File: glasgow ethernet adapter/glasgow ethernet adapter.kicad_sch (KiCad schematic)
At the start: 59 parts, among them J1 Glasgow Port, J2 RJ45_Amphenol_RJMG201K21120FR, U1 MxL86110, Y1 25 MHz

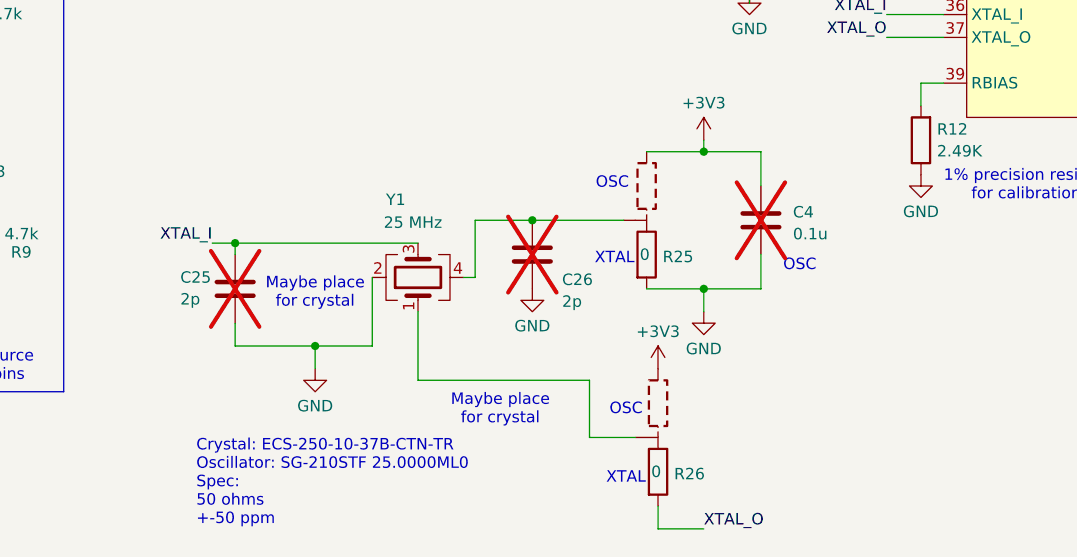
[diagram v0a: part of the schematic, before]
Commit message: export fab outputs, add note on parts sourcing
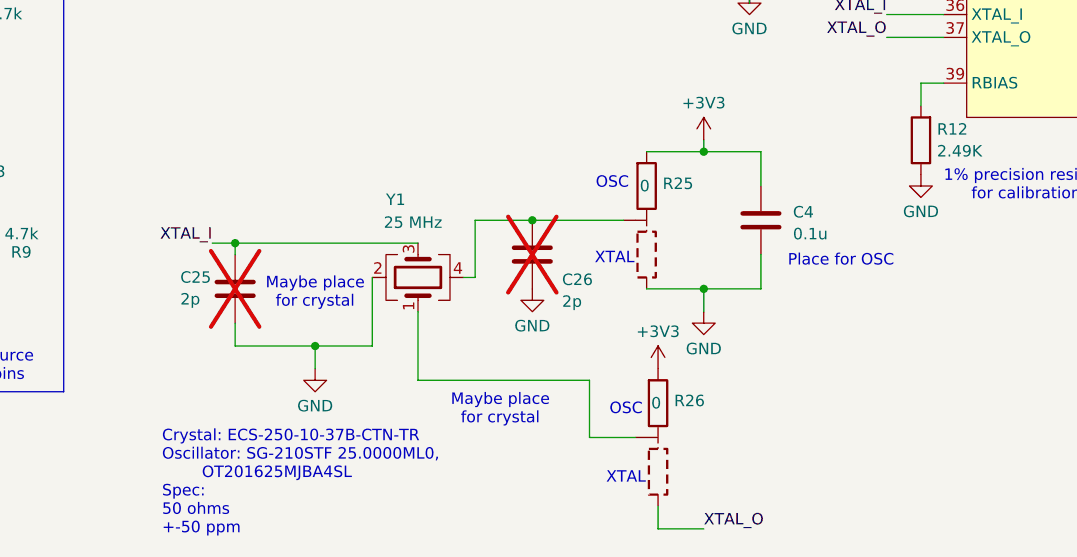
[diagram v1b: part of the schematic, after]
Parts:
- C4: now fitted
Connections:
- net +3V3: now also R25.1, R26.1; no longer R25.3, R26.3
- net GND: now also R25.3; no longer R25.1
- net XTAL_O: now also R26.3; no longer R26.1
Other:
- note added: "Crystal: ECS-250-10-37B-CTN-TR Oscillator: SG-210STF 25.0000ML0, OT201625MJBA4SL Spec: 50 ohms +-50 ppm"
- note added: "Place for OSC"
- note removed: "Crystal: ECS-250-10-37B-CTN-TR Oscillator: SG-210STF 25.0000ML0 Spec: 50 ohms +-50 ppm"
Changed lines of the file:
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@@
 	(text "OSC"
 		(exclude_from_sim no)
-		(at 160.528 166.37 0)
+		(at 139.7 157.226 0)
 		(effects
 			(font
@@
 		)
 	)
-	(text "OSC"
+	(text "Maybe place\nfor crystal\n"
 		(exclude_from_sim no)
-		(at 139.7 157.226 0)
+		(at 127.254 182.372 0)
 		(effects
 			(font
@@
 		)
 	)
-	(text "Maybe place\nfor crystal\n"
+	(text "Place for OSC"
 		(exclude_from_sim no)
-		(at 127.254 182.372 0)
+		(at 165.1 165.862 0)
 		(effects
 			(font
@@
 		)
 	)
-	(text "Crystal: ECS-250-10-37B-CTN-TR\nOscillator: SG-210STF 25.0000ML0\nSpec:\n50 ohms\n+-50 ppm"
+	(text "Crystal: ECS-250-10-37B-CTN-TR\nOscillator: SG-210STF 25.0000ML0, \n		OT201625MJBA4SL\nSpec:\n50 ohms\n+-50 ppm"
 		(exclude_from_sim no)
-		(at 93.472 190.5 0)
+		(at 89.662 190.5 0)
 		(effects
 			(font
@@
 		(in_bom yes)
 		(on_board yes)
-		(dnp yes)
+		(dnp no)
 		(property "Reference" "C4"
 			(at 159.766 160.3897 0)
@@
 	(symbol
 		(lib_id "glasgow:R-3-way")
-		(at 143.51 165.1 0)
-		(mirror x)
+		(at 143.51 157.48 0)
 		(unit 1)
 		(exclude_from_sim no)
@@
 		(dnp no)
 		(property "Reference" "R25"
-			(at 145.288 165.354 0)
+			(at 145.288 157.226 0)
 			(effects
 				(font
@@
 		)
 		(property "Value" "0"
-			(at 142.748 165.1 0)
+			(at 142.748 157.48 0)
 			(effects
 				(font
@@
 		)
 		(property "Footprint" "glasgow:R-3-Way_0402_1005Metric"
-			(at 141.732 165.1 90)
+			(at 141.732 157.48 90)
 			(effects
 				(font
@@
 		)
 		(property "Datasheet" "~"
-			(at 143.51 165.1 0)
+			(at 143.51 157.48 0)
 			(effects
 				(font
@@
 		)
 		(property "Description" "Resistor"
-			(at 143.51 165.1 0)
+			(at 143.51 157.48 0)
 			(effects
 				(font
@@
 	(symbol
 		(lib_id "glasgow:R-3-way")
-		(at 144.78 189.23 0)
-		(mirror x)
+		(at 144.78 181.61 0)
 		(unit 1)
 		(exclude_from_sim no)
@@
 		(dnp no)
 		(property "Reference" "R26"
-			(at 146.558 189.484 0)
+			(at 146.558 181.356 0)
 			(effects
 				(font
@@
 		)
 		(property "Value" "0"
-			(at 144.018 189.23 0)
+			(at 144.018 181.61 0)
 			(effects
 				(font
@@
 		)
 		(property "Footprint" "glasgow:R-3-Way_0402_1005Metric"
-			(at 143.002 189.23 90)
+			(at 143.002 181.61 90)
 			(effects
 				(font
@@
 		)
 		(property "Datasheet" "~"
-			(at 144.78 189.23 0)
+			(at 144.78 181.61 0)
 			(effects
 				(font
@@
 		)
 		(property "Description" "Resistor"
-			(at 144.78 189.23 0)
+			(at 144.78 181.61 0)
 			(effects
 				(font

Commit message: un-swap pins
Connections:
- net TRX1+: now also J2.2 (TD1+); no longer J2.10 (TD4-)
- net TRX1-: now also J2.3 (TD1-); no longer J2.9 (TD4+)
- net TRX2+: now also J2.4 (TD2+); no longer J2.8 (TD3-)
- net TRX2-: now also J2.5 (TD2-); no longer J2.7 (TD3+)
- net TRX3+: now also J2.7 (TD3+); no longer J2.5 (TD2-)
- net TRX3-: now also J2.8 (TD3-); no longer J2.4 (TD2+)
- net TRX4+: now also J2.9 (TD4+); no longer J2.3 (TD1-)
- net TRX4-: now also J2.10 (TD4-); no longer J2.2 (TD1+)
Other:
- note removed: "Pairs intentionally swapped for better routing"
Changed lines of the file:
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@@
-		)
-	)
-	(text "Pairs intentionally swapped \nfor better routing"
-		(exclude_from_sim no)
-		(at 267.208 59.69 0)
-		(effects
-			(font
-				(size 1.27 1.27)
-			)
 		)
 	)
@@
 	)
 	(label "TRX3+"
-		(at 259.08 88.9 180)
+		(at 259.08 91.44 180)
 		(fields_autoplaced yes)
 		(effects
@@
 	)
 	(label "TRX3-"
-		(at 259.08 83.82 180)
+		(at 259.08 96.52 180)
 		(fields_autoplaced yes)
 		(effects
@@
 	)
 	(label "TRX1+"
-		(at 259.08 104.14 180)
+		(at 259.08 76.2 180)
 		(fields_autoplaced yes)
 		(effects
@@
 	)
 	(label "TRX4-"
-		(at 259.08 76.2 180)
+		(at 259.08 104.14 180)
 		(fields_autoplaced yes)
 		(effects
@@
 	)
 	(label "TRX2+"
-		(at 259.08 96.52 180)
+		(at 259.08 83.82 180)
 		(fields_autoplaced yes)
 		(effects
@@
 	)
 	(label "TRX2-"
-		(at 259.08 91.44 180)
+		(at 259.08 88.9 180)
 		(fields_autoplaced yes)
 		(effects
@@
 	)
 	(label "TRX1-"
+		(at 259.08 81.28 180)
+		(fields_autoplaced yes)
+		(effects
+			(font
+				(size 1.27 1.27)
+			)
+			(justify right bottom)
+		)
+	)
+	(label "TRX4+"
 		(at 259.08 99.06 180)
 		(fields_autoplaced yes)
 		(effects
-			(font
-				(size 1.27 1.27)
-			)
-			(justify right bottom)
-		)
-	)
-	(label "TRX4+"
-		(at 259.08 81.28 180)
-		(fields_autoplaced yes)
-		(effects

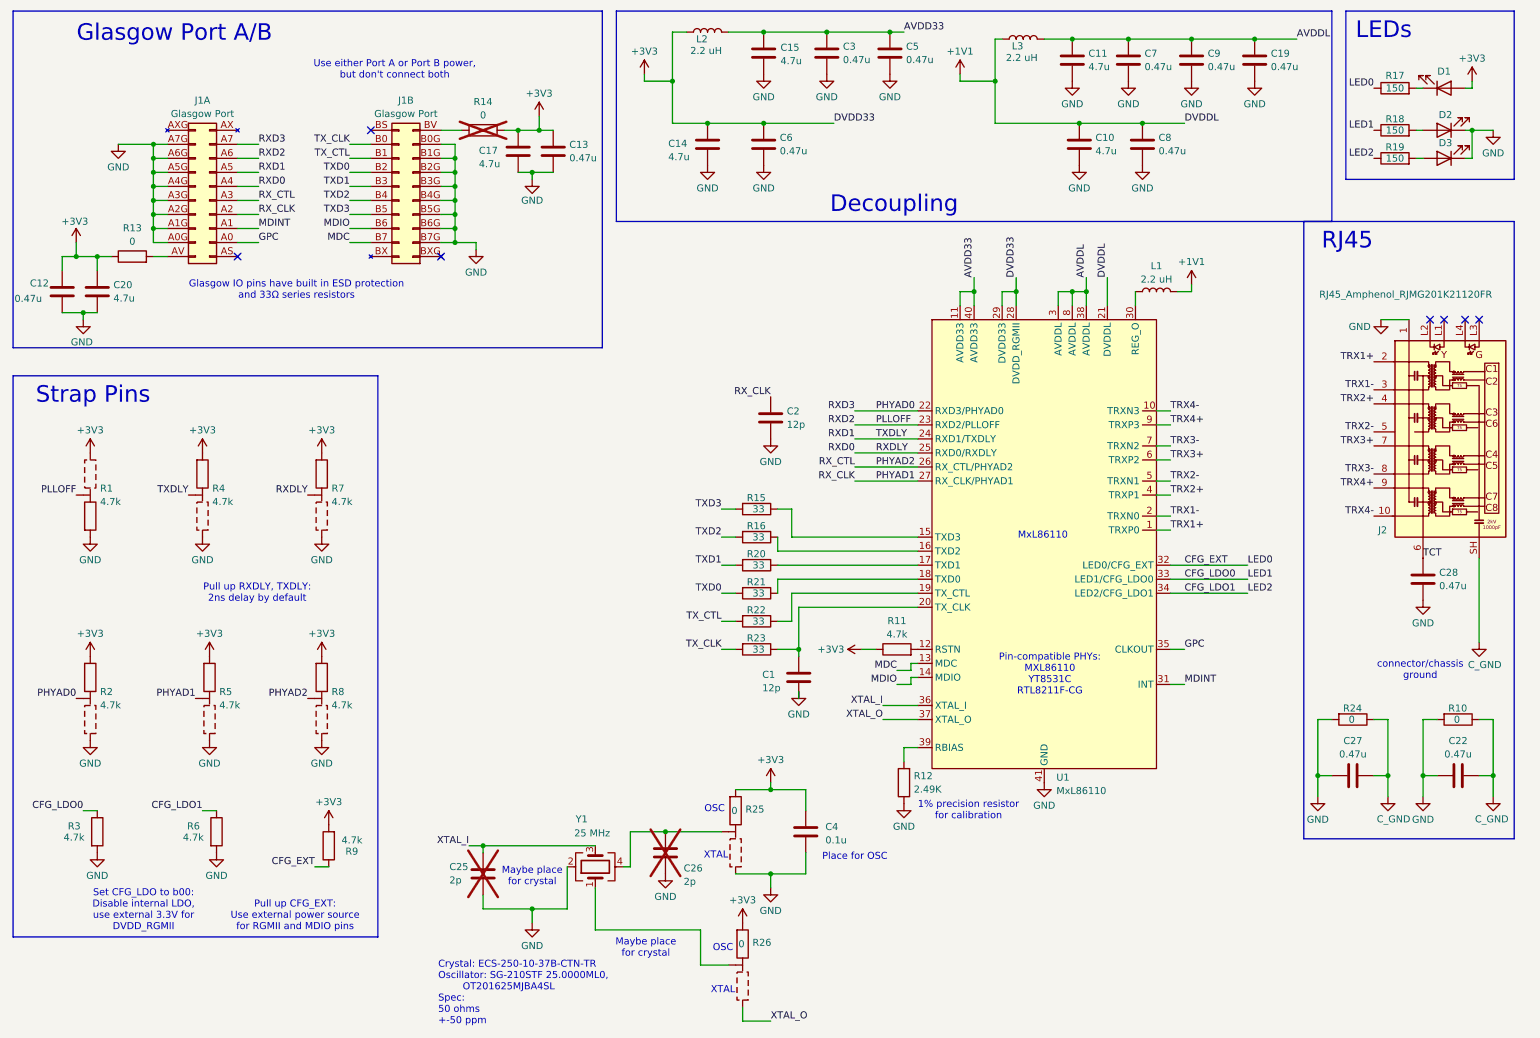
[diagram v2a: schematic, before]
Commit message: add 1v1 regulator
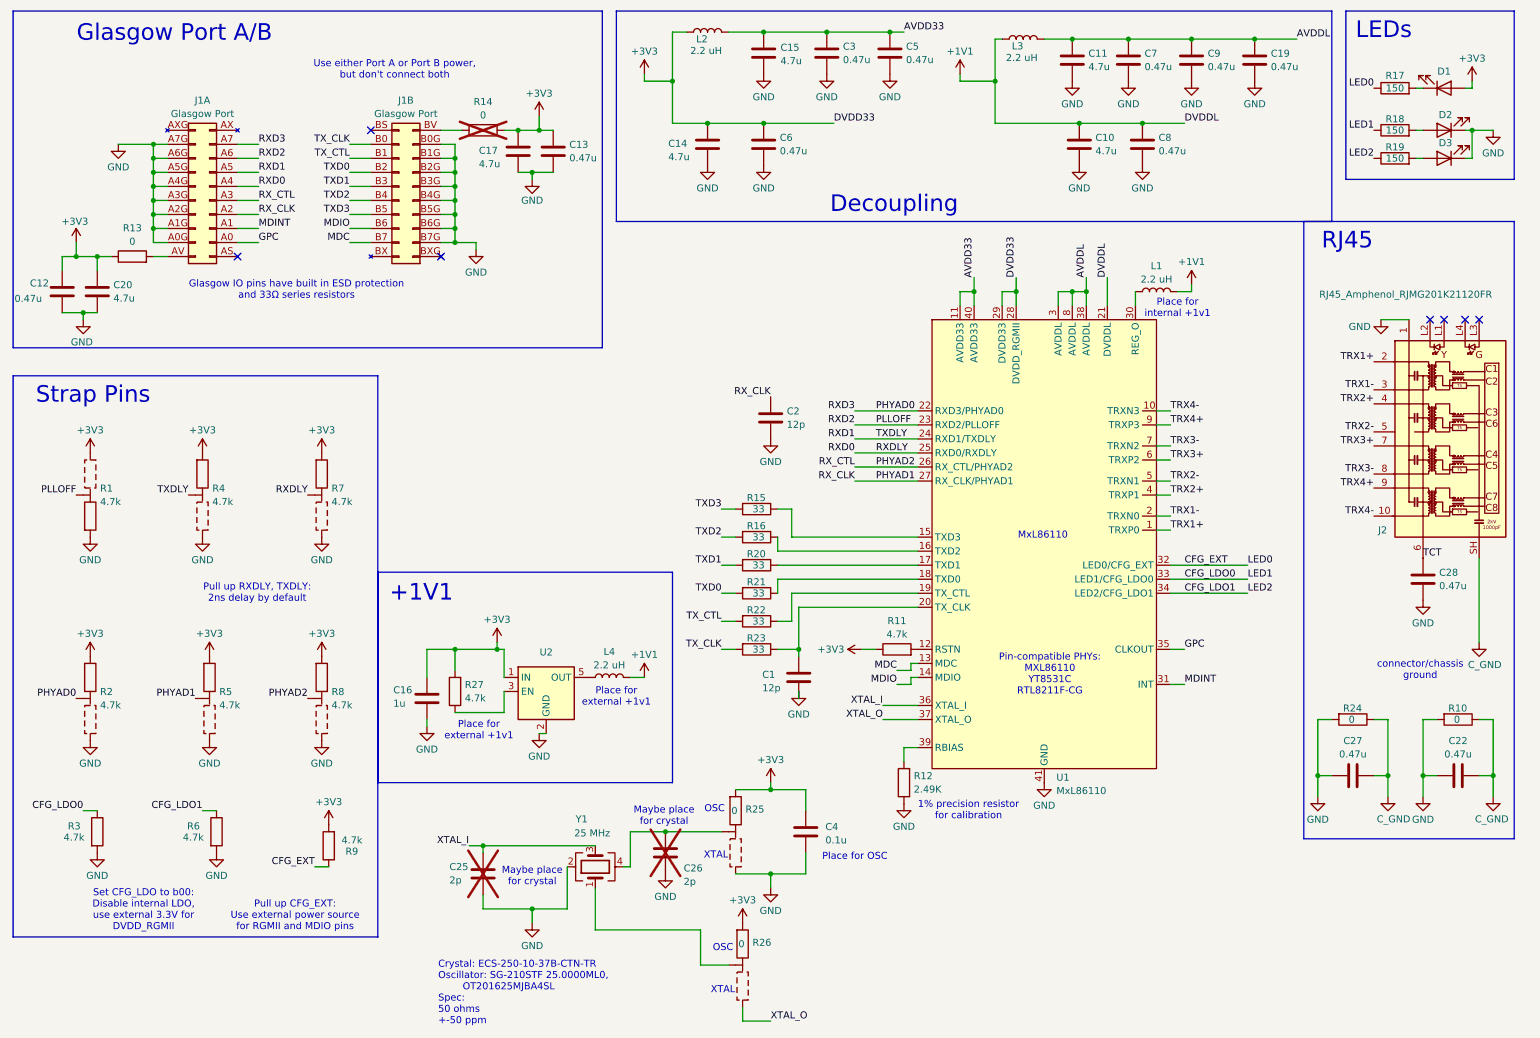
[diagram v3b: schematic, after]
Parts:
- added C16: 1u, Capacitor_SMD:C_0603_1608Metric, symbol Device:C
- added L4: 2.2 uH, Inductor_SMD:L_0603_1608Metric, symbol Device:L
- added R27: 4.7k, Resistor_SMD:R_0402_1005Metric, symbol Device:R
- added U2: ~, Package_TO_SOT_SMD:SOT-23-5, symbol glasgow:TLV74311PDBVR
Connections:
- net +1V1: now also L4.2
- net +3V3: now also C16.1, R27.2, U2.1 (IN)
- net GND: now also C16.2, U2.2 (GND)
- new net: R27.1, U2.3 (EN)
- new net: L4.1, U2.5 (OUT)
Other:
- note added: "+1V1"
- note added: "Place for external +1v1"
- note added: "Place for internal +1v1"

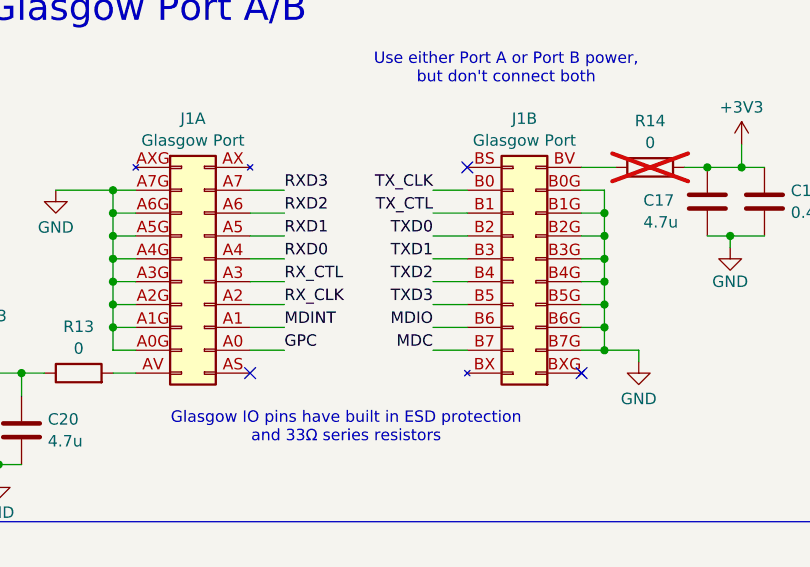
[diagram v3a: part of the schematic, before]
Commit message: swap MDC+MDIO with TXD0:3
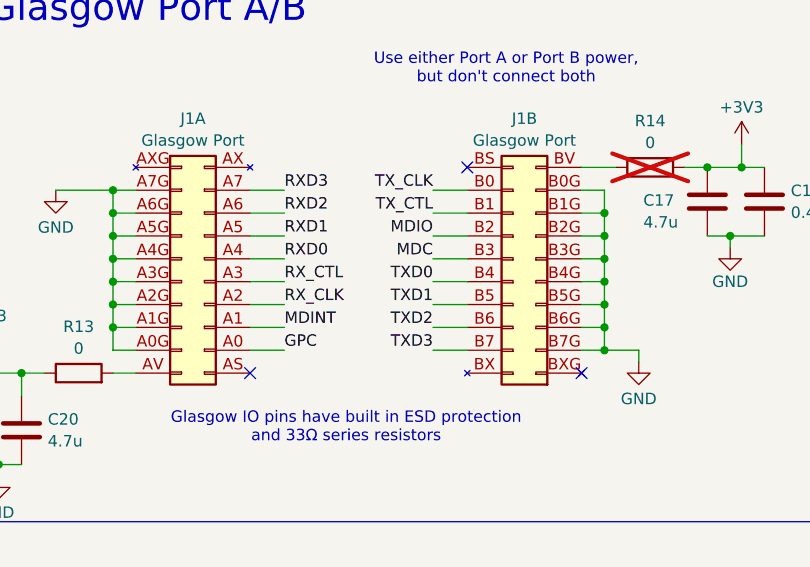
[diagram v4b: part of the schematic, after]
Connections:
- net MDC: now also J1.B3; no longer J1.B7
- net MDIO: now also J1.B2; no longer J1.B6
- net TXD0: now also J1.B4; no longer J1.B2
- net TXD1: now also J1.B5; no longer J1.B3
- net TXD2: now also J1.B6; no longer J1.B4
- net TXD3: now also J1.B7; no longer J1.B5
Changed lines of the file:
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@@
 	)
 	(label "TXD1"
-		(at 73.66 44.45 180)
+		(at 73.66 49.53 180)
 		(fields_autoplaced yes)
 		(effects
@@
 	)
 	(label "TXD2"
-		(at 73.66 46.99 180)
+		(at 73.66 52.07 180)
 		(fields_autoplaced yes)
 		(effects
@@
 	)
 	(label "MDIO"
-		(at 73.66 52.07 180)
+		(at 73.66 41.91 180)
 		(fields_autoplaced yes)
 		(effects
@@
 	)
 	(label "TXD3"
-		(at 73.66 49.53 180)
+		(at 73.66 54.61 180)
 		(fields_autoplaced yes)
 		(effects
@@
 	)
 	(label "MDC"
-		(at 73.66 54.61 180)
+		(at 73.66 44.45 180)
 		(fields_autoplaced yes)
 		(effects
@@
 	)
 	(label "TXD0"
-		(at 73.66 41.91 180)
-		(fields_autoplaced yes)
-		(effects
+		(at 73.66 46.99 180)
+		(fields_autoplaced yes)
+		(effects

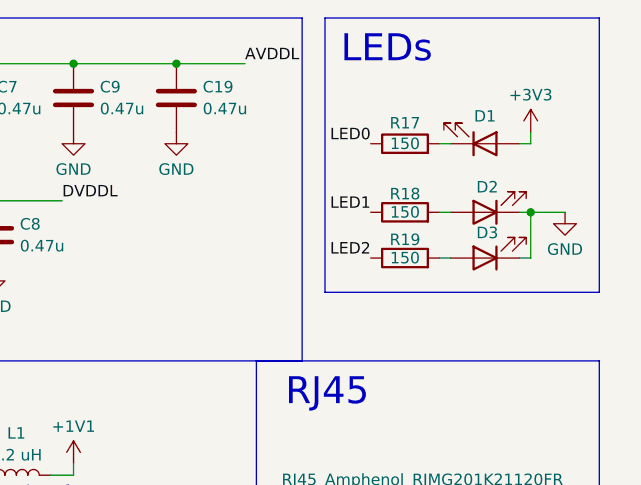
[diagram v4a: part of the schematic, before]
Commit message: individually identify LEDs (to assign colors in BOM)
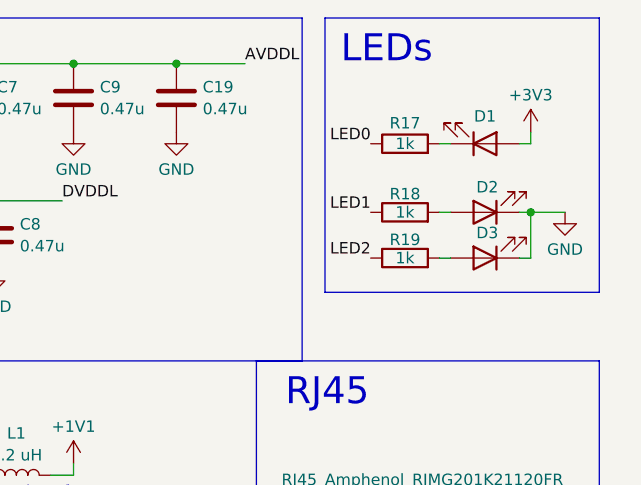
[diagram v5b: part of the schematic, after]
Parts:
- D1: value LED -> LED_0
- D2: value LED -> LED_1
- D3: value LED -> LED_3
- R17, R18, R19: value 150 -> 1k
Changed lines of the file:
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@@
 			)
 		)
-		(property "Value" "LED"
+		(property "Value" "LED_0"
 			(at 270.1925 22.7908 0)
 			(effects
@@
 			)
 		)
-		(property "Value" "150"
+		(property "Value" "1k"
 			(at 262.89 26.67 90)
 			(effects
@@
 			)
 		)
-		(property "Value" "LED"
+		(property "Value" "LED_3"
 			(at 273.3675 35.4908 0)
 			(effects
@@
 			)
 		)
-		(property "Value" "150"
+		(property "Value" "1k"
 			(at 262.89 39.37 90)
 			(effects
@@
 			)
 		)
-		(property "Value" "LED"
+		(property "Value" "LED_1"
 			(at 273.3675 30.4108 0)
 			(effects
@@
 			)
 		)
-		(property "Value" "150"
+		(property "Value" "1k"
 			(at 262.89 34.29 90)
 			(effects
